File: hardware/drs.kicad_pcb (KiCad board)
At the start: 2 copper layers, 60 x 40 mm, 91 parts, among them IC1 LMR38020FDDAR, J1 USB-C_GCT_USB4145-03-0070-C, J2 FTSH-107-01-L-D-K, J3 POWER & CAN & SPI2, J4 PWM1, J5 PWM2, Q1 LMR51635XDDCR, Q2 LMR51635XDDCR, T1 TP_VCC, T10 TP_+3V3, T11 TP_+5V, T12 TP_+5V, T13 TP_VBUS, T14 TP_+3V3, T15 TP_+5V, T16 TP_CAN_H, T17 TP_CAN_L, T2 TP_VCC, T3 TP_VCC, T4 TP_VCC, T5 TP_+6V6S1, T6 TP_+6V6S1, T7 TP_+6V6S2, T8 TP_+6V6S2, U1 STM32G0C1KCTxN, U2 LM1117-3.3, U3 MCP2542FDxMF

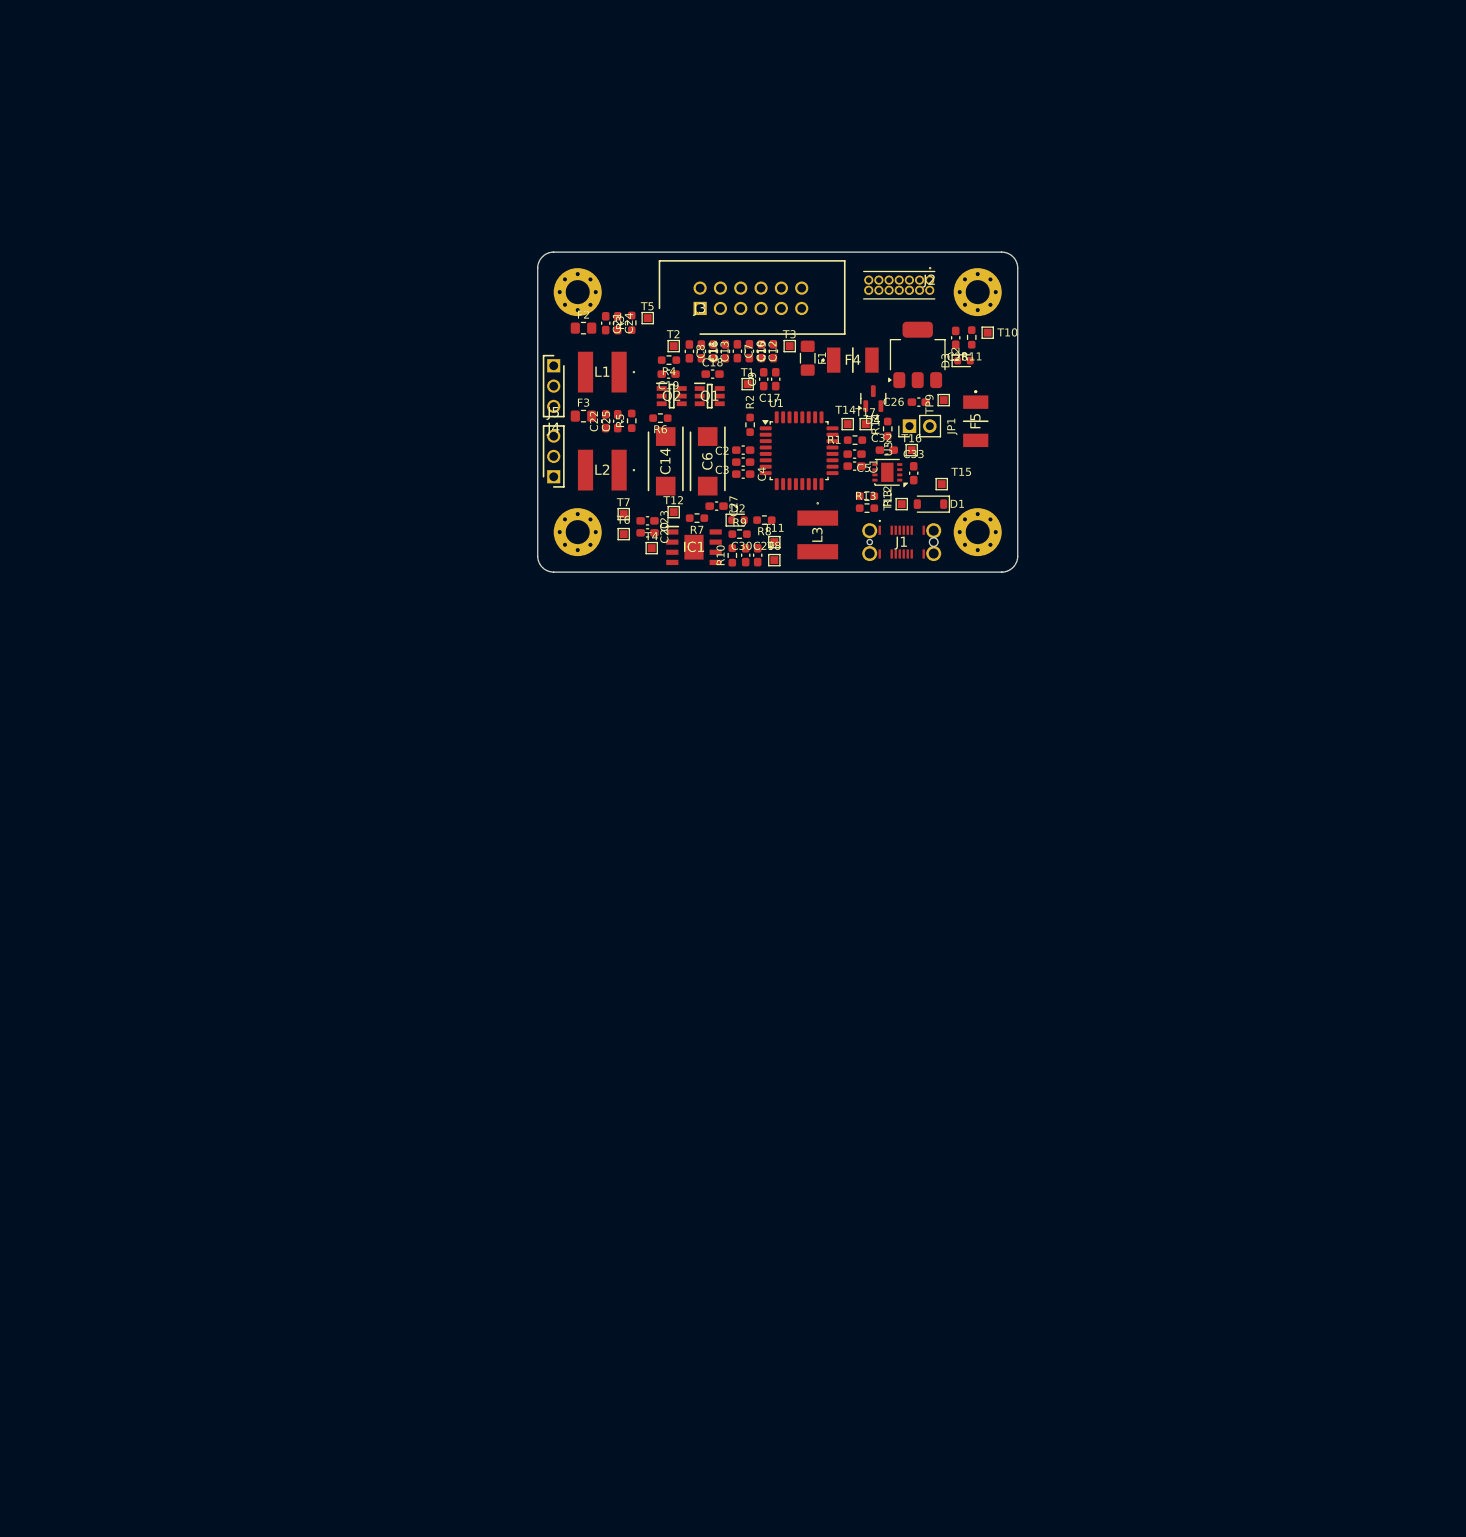
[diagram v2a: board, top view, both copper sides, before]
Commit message: Wszystkie elementy poukładane według dokumentacji na pod-grupy
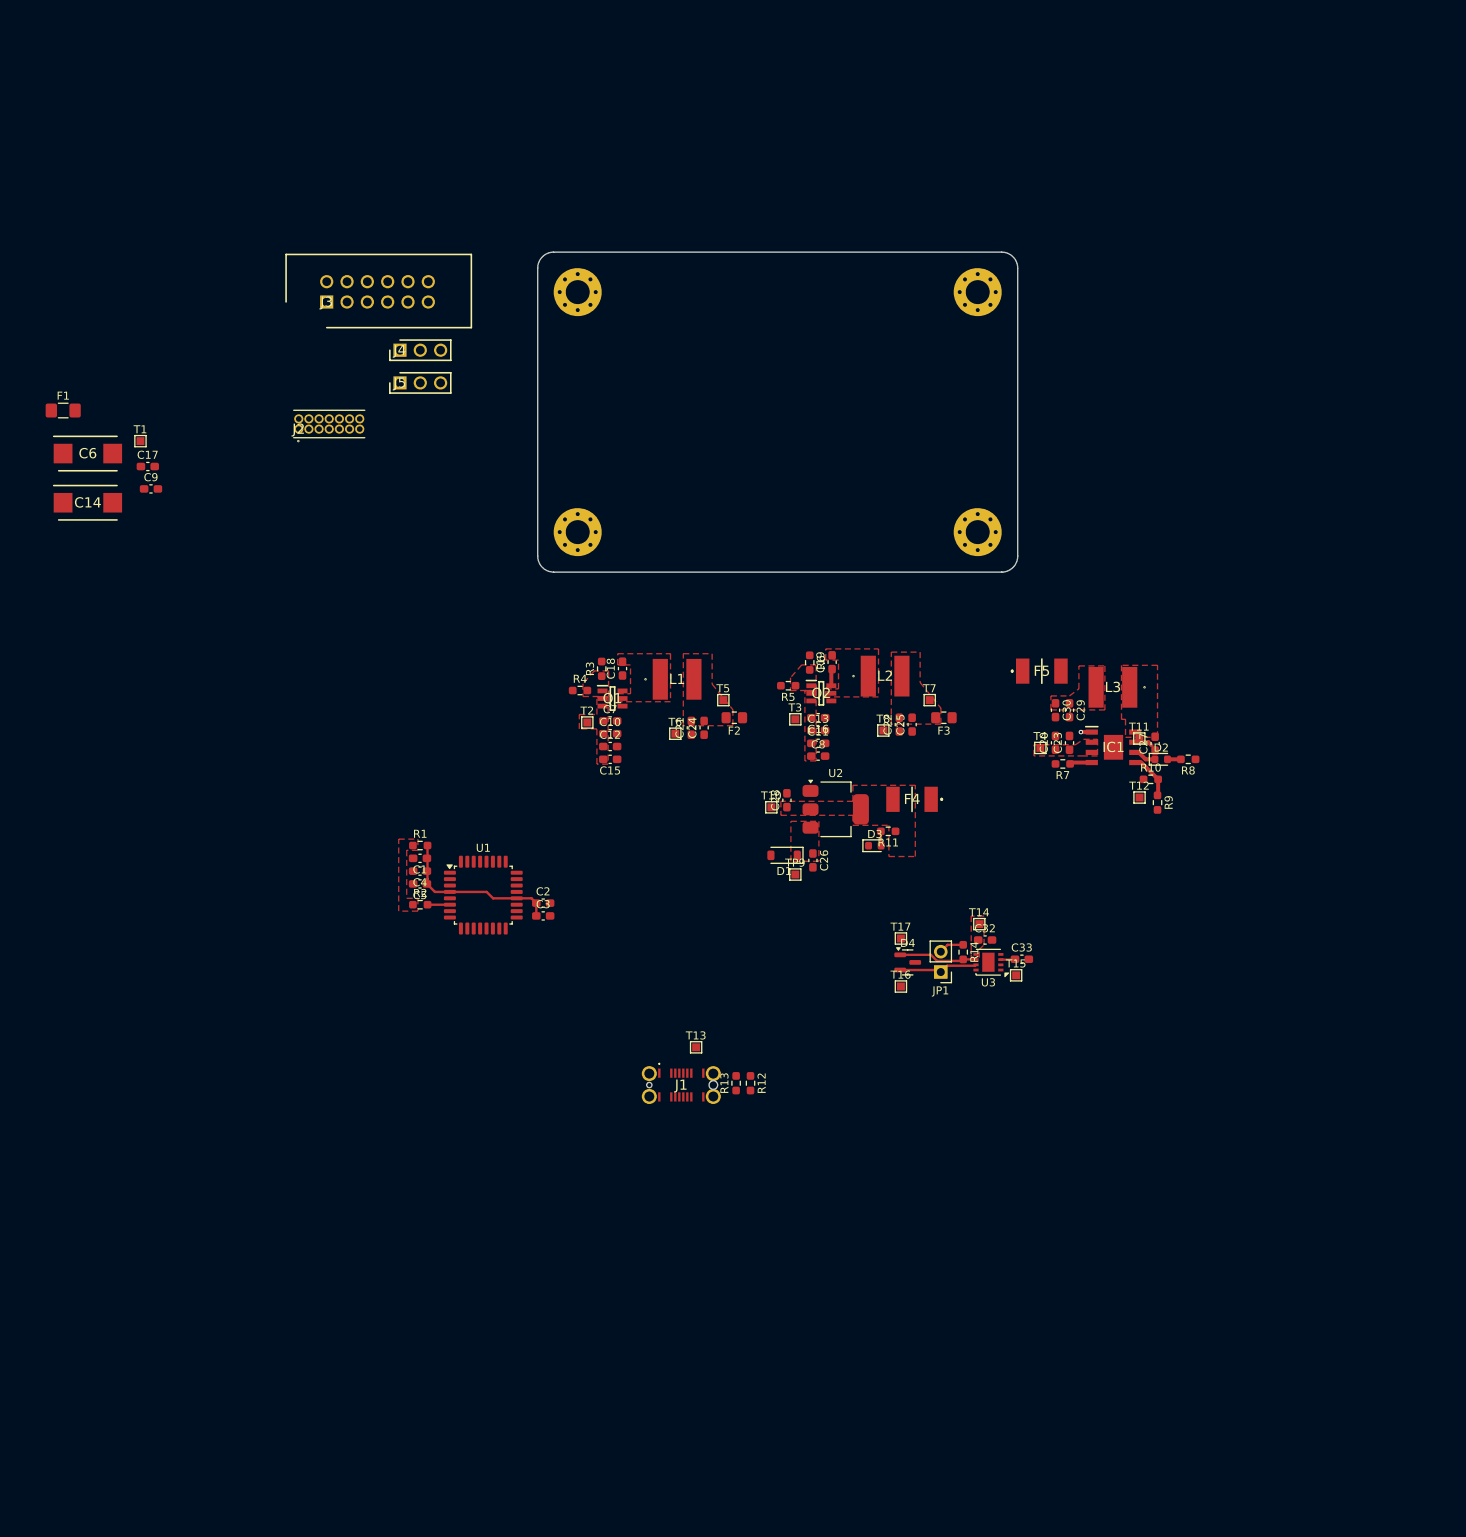
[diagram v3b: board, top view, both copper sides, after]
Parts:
- moved F1 93.3 mm to (56.7, 95.8), turned to 0 degrees
- moved J2 81.0 mm to (86.1, 98.1), turned to 0 degrees
- moved C17 79.2 mm to (67.3, 102.8), turned to 0 degrees
- moved C9 77.8 mm to (67.7, 105.6), turned to 0 degrees
- moved C6 77.5 mm to (59.8, 101.2), turned to 0 degrees
- moved C5 76.4 mm to (101.3, 155.0), turned to 180 degrees
- moved T1 76.2 mm to (66.3, 99.6)
- moved R12 74.8 mm to (142.6, 179.9), turned to -90 degrees
- moved R1 74.3 mm to (101.3, 150.2), turned to 0 degrees
- moved R13 73.7 mm to (140.8, 179.9), turned to 90 degrees
- moved J1 73.2 mm to (133.9, 180.1)
- moved C1 73.2 mm to (101.3, 151.8), turned to 180 degrees
- moved R2 72.8 mm to (101.3, 157.6), turned to 0 degrees
- moved T13 72.6 mm to (135.8, 175.4)
- moved C14 72.4 mm to (59.8, 107.3), turned to 0 degrees
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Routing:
- net /Control/STM_VCC: track 0.00 -> 21.1 mm
- net CAN_H: track 0.00 -> 9.95 mm
- net CAN_L: track 0.00 -> 9.88 mm
- net /Power/FB_+5V: track 0.00 -> 5.76 mm
- net /Power/GND_IC1: track 0.00 -> 4.15 mm, vias 0 -> 1
- net /CAN/JP1_to_R6: track 0.00 -> 3.16 mm
- net /Power/PG_+5V: track 0.00 -> 2.82 mm
- net /Control/NRST: track 0.00 -> 2.80 mm
- net /Power/BOOT_+5V: track 0.00 -> 2.20 mm
- net /Power/CB_+6V6S2: track 0.00 -> 2.12 mm
- net /Power/D2_to_R14: track 0.00 -> 1.81 mm
- net +5V: track 0.00 -> 1.80 mm
- net /Power/D3_to_R8: track 0.00 -> 1.68 mm
- added copper zone on F.Cu, net +3V3
- added copper zone on F.Cu, net +5V
- added copper zone on F.Cu, net /Power/+6V6S2_OUT
- added copper zone on F.Cu, net /Power/FB_+6V6S2
- added copper zone on F.Cu, net /Power/FUSE_+5V
- added copper zone on F.Cu, net /Power/SW_+5V
- added copper zone on F.Cu, net /Power/SW_+6V6S2
- added copper zone on F.Cu, net /Power/VO_+3.3V
- added copper zone on F.Cu, net VCC

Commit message: nowy uklad
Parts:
- F4, F5: footprint SamacSys_Parts:MINIASMDC260F162 -> Fuse:Fuse_1812_4532Metric_Pad1.30x3.40mm_HandSolder
- IC1: footprint SamacSys_Parts:SOIC127P600X170-9N -> Package_SO:SOIC-8-1EP_3.9x4.9mm_P1.27mm_EP2.29x3mm
- L1, L2, L3: footprint SamacSys_Parts:VLS6045 -> Inductor_SMD:L_TDK_VLS6045EX_VLS6045AF
- Q1: footprint SamacSys_Parts:SOT95P280X110-6N -> Package_TO_SOT_SMD:SOT-23-6_Handsoldering
- moved T15 98.4 mm to (95.3, 109.8), turned to 90 degrees
- moved R8 94.2 mm to (104.1, 126.2), turned to 0 degrees
- moved C33 93.0 mm to (123.0, 88.4)
- moved R9 88.2 mm to (107.9, 123.8), turned to 180 degrees
- moved U3 87.8 mm to (122.9, 92.2), turned to -90 degrees
- moved D2 87.5 mm to (107.4, 126.2), turned to 180 degrees
- moved C32 86.6 mm to (120.2, 92.6), turned to 90 degrees
- moved T14 85.2 mm to (118.2, 93.3), turned to 90 degrees
- moved C27 84.8 mm to (108.8, 128.7), turned to -90 degrees
- moved R14 83.1 mm to (121.7, 95.3), turned to 0 degrees
- moved R10 83.0 mm to (111.7, 123.8), turned to 180 degrees
- moved JP1 79.9 mm to (124.2, 98.1), turned to -90 degrees
- moved IC1 75.3 mm to (113.4, 127.7), turned to 180 degrees
- moved L3 74.7 mm to (113.3, 134.2), turned to 0 degrees
- moved D4 73.8 mm to (123.0, 102.3), turned to 90 degrees
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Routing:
- net GND: track 0.00 -> 6.36 mm, vias 0 -> 16
- net /Control/STM_VCC: track 21.1 -> 16.8 mm
- net /Power/FB_+6V6S1: track 0.00 -> 3.97 mm
- net /Power/FB_+6V6S2: track 0.00 -> 3.68 mm
- net /Power/CB_+6V6S1: track 0.00 -> 2.23 mm
- net /Power/FB_+5V: track 5.76 -> 4.04 mm
- net +5V: track 1.80 -> 2.47 mm
- net /Power/SW_+6V6S2: vias 0 -> 1
- net /Power/SW_+6V6S1: vias 0 -> 11
- added copper zone on F.Cu, net /Power/+6V6S1_OUT
- added copper zone on B.Cu, net /Power/SW_+6V6S1
- added copper zone on F.Cu, net /Power/SW_+6V6S1
- added copper zone on B.Cu, net GND
- added copper zone on F.Cu, net GND
- removed copper zone on F.Cu, net /Power/+6V6S2_OUT
- removed copper zone on F.Cu, net /Power/FB_+6V6S2
- removed copper zone on F.Cu, net /Power/SW_+6V6S2
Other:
- copper layers 2 -> 4

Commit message: update
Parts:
- moved T14 58.1 mm to (164.6, 128.4)
- moved D4 58.1 mm to (169.4, 137.3)
- moved R14 58.1 mm to (168.1, 130.4)
- moved C32 58.1 mm to (166.6, 127.6)
- moved C33 58.1 mm to (169.4, 123.4)
- moved JP1 58.1 mm to (170.6, 133.2)
- moved T16 58.1 mm to (172.4, 138.2)
- moved T17 58.1 mm to (166.4, 138.2)
- moved U3 58.1 mm to (169.3, 127.2)
- moved J1 51.6 mm to (113.5, 132.7)
- moved T13 51.6 mm to (115.4, 128.0)
- moved R13 51.6 mm to (120.4, 132.5)
- moved R12 51.6 mm to (122.2, 132.5)
- moved C27 37.6 mm to (124.2, 94.5)
- moved D2 37.6 mm to (122.9, 91.9)
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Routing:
- net /Power/GND_IC1: track 4.15 -> 10.1 mm, vias 1 -> 2

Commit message: schematic & pcb update
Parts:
- added C24: 22u, Capacitor_SMD:C_0805_2012Metric, F.Cu at (151.8, 62.8)
- added C25: 100n, Capacitor_SMD:C_0603_1608Metric, F.Cu at (154.0, 63.0)
- added C27: 100n, Capacitor_SMD:C_0603_1608Metric_Pad1.08x0.95mm_HandSolder, F.Cu at (161.0, 59.8)
- added C28: 22u, Capacitor_SMD:C_0805_2012Metric, F.Cu at (150.3, 53.6)
- added C30: 22u, Capacitor_SMD:C_0805_2012Metric, F.Cu at (150.3, 51.4)
- added C31: 22u, Capacitor_SMD:C_0805_2012Metric, F.Cu at (150.3, 49.2)
- added D1: LED_WRN, LED_SMD:LED_0603_1608Metric, F.Cu at (184.0, 124.0)
- added D2: LED_OK, LED_SMD:LED_0603_1608Metric, F.Cu at (184.0, 120.5)
- added D3: LED_ERR, LED_SMD:LED_0603_1608Metric, F.Cu at (184.0, 122.2)
- added D4: 600W/28V, Diode_SMD:D_SOD-323_HandSoldering, F.Cu at (89.4, 73.8)
- added D5: 9V1, Diode_SMD:D_SOD-323_HandSoldering, F.Cu at (94.6, 77.8)
- added IC1: TPS54202HDDCR, Package_TO_SOT_SMD:SOT-23-6, F.Cu at (158.8, 62.5)
- added L3: 68u/1A4, Inductor_SMD:L_TDK_VLS6045EX_VLS6045AF, F.Cu at (147.2, 58.2)
- added Q1: SI2347DS-T1-GE3, Package_TO_SOT_SMD:SOT-23_Handsoldering, F.Cu at (94.7, 74.8)
- added R11: 510k, Resistor_SMD:R_0603_1608Metric, F.Cu at (162.8, 62.4)
- added R12: 13k3, Resistor_SMD:R_0603_1608Metric, F.Cu at (165.3, 62.6)
- added R13: 100k, Resistor_SMD:R_0603_1608Metric, F.Cu at (167.2, 62.6)
- added R2: 1k, Resistor_SMD:R_0603_1608Metric_Pad0.98x0.95mm_HandSolder, F.Cu at (180.5, 124.0)
- added R3: 1k, Resistor_SMD:R_0603_1608Metric_Pad0.98x0.95mm_HandSolder, F.Cu at (180.5, 120.5)
- added R4: 1k, Resistor_SMD:R_0603_1608Metric_Pad0.98x0.95mm_HandSolder, F.Cu at (180.5, 122.2)
- added R6: 100k, Resistor_SMD:R_0603_1608Metric_Pad0.98x0.95mm_HandSolder, F.Cu at (89.8, 75.8)
- F5: footprint Fuse:Fuse_1812_4532Metric_Pad1.30x3.40mm_HandSolder -> SamacSys_Parts:MINIASMDC260F162
- L2: footprint Inductor_SMD:L_TDK_VLS6045EX_VLS6045AF -> SamacSys_Parts:VLS6045
- moved T3 143.4 mm to (143.9, 220.2)
- moved T1 114.6 mm to (150.7, 214.1)
- moved T14 114.6 mm to (140.2, 215.2)
- moved T2 114.6 mm to (150.7, 216.7)
- moved T7 114.1 mm to (145.5, 214.5), turned to 90 degrees
- moved T4 108.8 mm to (56.2, 98.5), turned to 90 degrees
- moved F2 107.6 mm to (58.5, 97.8), turned to -90 degrees
- moved T13 105.4 mm to (126.2, 226.5), turned to 0 degrees
- moved L1 103.6 mm to (56.2, 103.4), turned to 90 degrees
- moved C22 102.8 mm to (61.6, 99.7), turned to 180 degrees
- moved T12 101.5 mm to (146.0, 224.8)
- moved C20 101.0 mm to (61.6, 101.2), turned to 180 degrees
- moved C18 101.0 mm to (53.2, 109.0), turned to 90 degrees
- moved T5 98.3 mm to (62.2, 103.2), turned to 90 degrees
- moved R7 97.9 mm to (53.5, 113.1), turned to -90 degrees
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- renumbered C12 to C10, C13 to C11, C15 to C12, C16 to C13, C6 to C14, C9 to C15, C14 to C16, C21 to C20, C22 to C21, C24 to C22, C25 to C23, C27 to C26, C28 to C29, C7 to C6, C8 to C7, C10 to C8, C11 to C9, D1 to D6, D3 to D7, D4 to D8, Q1 to Q2, Q2 to Q3, R6 to R10, R11 to R14, R12 to R15, R13 to R16, R14 to R17, R2 to R5, R3 to R7, R4 to R8, R5 to R9, T2 to T1, T12 to T10, T10 to T11, T13 to T12, T14 to T13, T15 to T14, T16 to T15, T17 to T16, T3 to T2, T1 to T3, T5 to T4, T6 to T5, T7 to T6, T8 to T7, T4 to T8, T11 to T9, TP9 to TP1
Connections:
- net /Power/D2_to_R14 renamed /Power/D3V3_to_R1k
- C14 pad 1: /Power/VCC_IN -> VCC
- C15 pad 1: /Power/VCC_IN -> VCC
- C16 pad 1: /Power/VCC_IN -> VCC
- C17 pad 1: /Power/VCC_IN -> VCC
- C26 pad 1: /Power/BOOT_+5V -> Net-(IC1-BOOT)
- C26 pad 2: /Power/SW_+5V -> /Power/SW
- F1 pad 2: /Power/VCC_IN -> /Power/RPP_D
- F5 pad 2: /Power/FUSE_+5V -> /Power/+5V_OUT
- J3 pad 6: unconnected-(J3-Pin_6-Pad6) -> CAN_H
- T3 pad 1: /Power/VCC_IN -> /Power/RPP_D
- T9 pad 1: /Power/FUSE_+5V -> /Power/+5V_OUT
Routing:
- net /Power/FB_+5V: track 4.04 -> 9.17 mm
- net /Control/LED_OK: track 0.00 -> 4.67 mm
- net /Control/LED_ERR: track 0.00 -> 2.95 mm
- net /Power/BOOT_+5V: track 2.34 -> 5.06 mm
- net /Control/LED_WRN: track 0.00 -> 2.60 mm
- net GND: track 6.36 -> 3.85 mm
- net +5V: track 2.47 -> 0.00 mm
- net /Control/DWRN_to_R1k: track 0.00 -> 1.80 mm
- net /Control/DOK_to_R1k: track 0.00 -> 1.80 mm
- net /Control/DERR_to_R1k: track 0.00 -> 1.80 mm
- net /Power/FUSE_+5V: track 0.00 -> 1.67 mm
- net /Power/SW_+5V: vias 0 -> 9
- added copper zone on In2.Cu, net (none)
- added copper zone on F.Cu, net /Power/+5V_OUT
- added copper zone on B.Cu, net /Power/SW_+5V
- added copper zone on In1.Cu, net GND
- removed copper zone on F.Cu, net /Power/FUSE_+5V

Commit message: schematic & pcb udpate
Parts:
- removed the C20 at (203.0, 103.9)
- removed the C23 at (201.3, 103.9)
- removed the C26 at (191.2, 104.4)
- removed the C29 at (201.3, 108.0)
- removed the C30 at (203.0, 108.0)
- removed the D2 at (191.0, 100.9)
- removed the IC1 at (195.8, 103.3)
- removed the L3 at (195.7, 109.8)
- removed the R10 at (200.6, 99.6)
- removed the R7 at (202.1, 101.3)
- removed the R8 at (193.6, 99.6)
- removed the R9 at (197.1, 99.6)
- F5: footprint SamacSys_Parts:MINIASMDC260F162 -> Fuse:Fuse_1812_4532Metric_Pad1.30x3.40mm_HandSolder
- L2: footprint SamacSys_Parts:VLS6045 -> Inductor_SMD:L_TDK_VLS6045EX_VLS6045AF
- moved T1 145.6 mm to (218.8, 85.3)
- moved T10 145.6 mm to (228.3, 94.2)
- moved T12 145.6 mm to (214.1, 96.0)
- moved T13 145.6 mm to (194.3, 97.8)
- moved T14 145.6 mm to (208.3, 86.5)
- moved T15 145.6 mm to (200.6, 96.8)
- moved T16 145.6 mm to (205.8, 100.3)
- moved T2 145.6 mm to (218.8, 88.0)
- moved T3 145.6 mm to (212.0, 91.5)
- moved T7 145.6 mm to (213.6, 85.8)
- moved T9 145.6 mm to (191.9, 105.2)
- moved TP1 145.6 mm to (198.7, 101.8)
- moved T4 113.7 mm to (169.5, 88.7), turned to 0 degrees
- moved F2 112.0 mm to (170.3, 91.0), turned to 180 degrees
- moved L1 109.4 mm to (164.7, 88.7), turned to 0 degrees
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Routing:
- net /Power/+5V_OUT: track 0.00 -> 15.0 mm
- net /Power/GND_IC1: track 10.1 -> 0.00 mm, vias 2 -> 0
- net /Power/SW_+5V: track 0.00 -> 8.47 mm, vias 9 -> 0
- net VCC: track 0.00 -> 6.24 mm
- net /Power/FB_+5V: track 9.17 -> 3.76 mm
- net GND: track 3.85 -> 8.06 mm
- net /Power/EN: track 0.00 -> 4.05 mm
- net /Power/BOOT_+5V: track 5.06 -> 1.83 mm
- net /Power/PG_+5V: track 2.71 -> 0.00 mm
- net /Power/D3_to_R8: track 1.88 -> 0.00 mm
- net /Power/FUSE_+5V: track 1.67 -> 0.00 mm
- removed copper zone on F.Cu, net /Power/+5V_OUT
- removed copper zone on B.Cu, net /Power/SW_+5V
- removed copper zone on F.Cu, net /Power/SW_+5V

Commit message: pcb update
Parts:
- moved D7 3.24 mm to (147.8, 107.2)
- moved R14 2.45 mm to (144.5, 107.2)
- moved F4 1.66 mm to (142.8, 111.2), turned to -90 degrees
- moved D5 1.18 mm to (125.6, 109.8), turned to 90 degrees
- moved C29 0.77 mm to (154.8, 112.8)
- moved C14 0.25 mm to (120.8, 89.5)
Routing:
- net /Power/RPP_D: track 0.00 -> 7.18 mm
- net /Power/RPP_G: track 0.00 -> 5.32 mm
- net +3V3: track 0.00 -> 3.39 mm
- net /Power/D3V3_to_R1k: track 1.77 -> 0.00 mm
- net GND: track 8.06 -> 9.81 mm
- net +5V: track 0.00 -> 1.72 mm
- removed copper zone on F.Cu, net +3V3
